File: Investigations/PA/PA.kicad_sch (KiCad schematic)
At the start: 6 parts, among them Q1 BS170

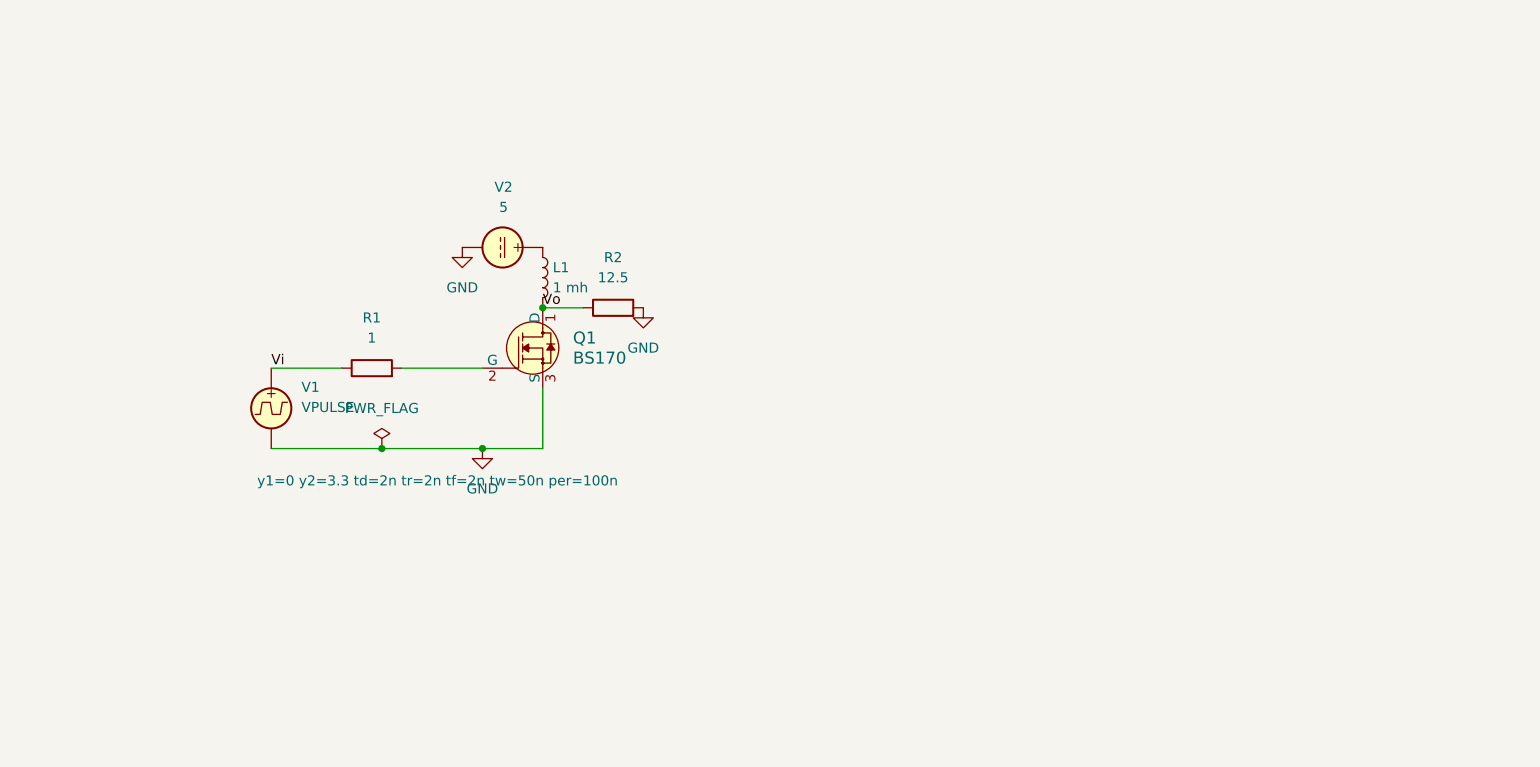
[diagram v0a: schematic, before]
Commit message: Created Pocket FT8 Proto PA
Prototype of a ~1W PA using BS170s with Vcc=5V for a future version of the transceiver.  The low-pass filter can be implemented as a Butterworth with a harmonic trap, or as a Chebyshev without a trap.  Investigations folder has simulations of assorted filter designs/frequencies.
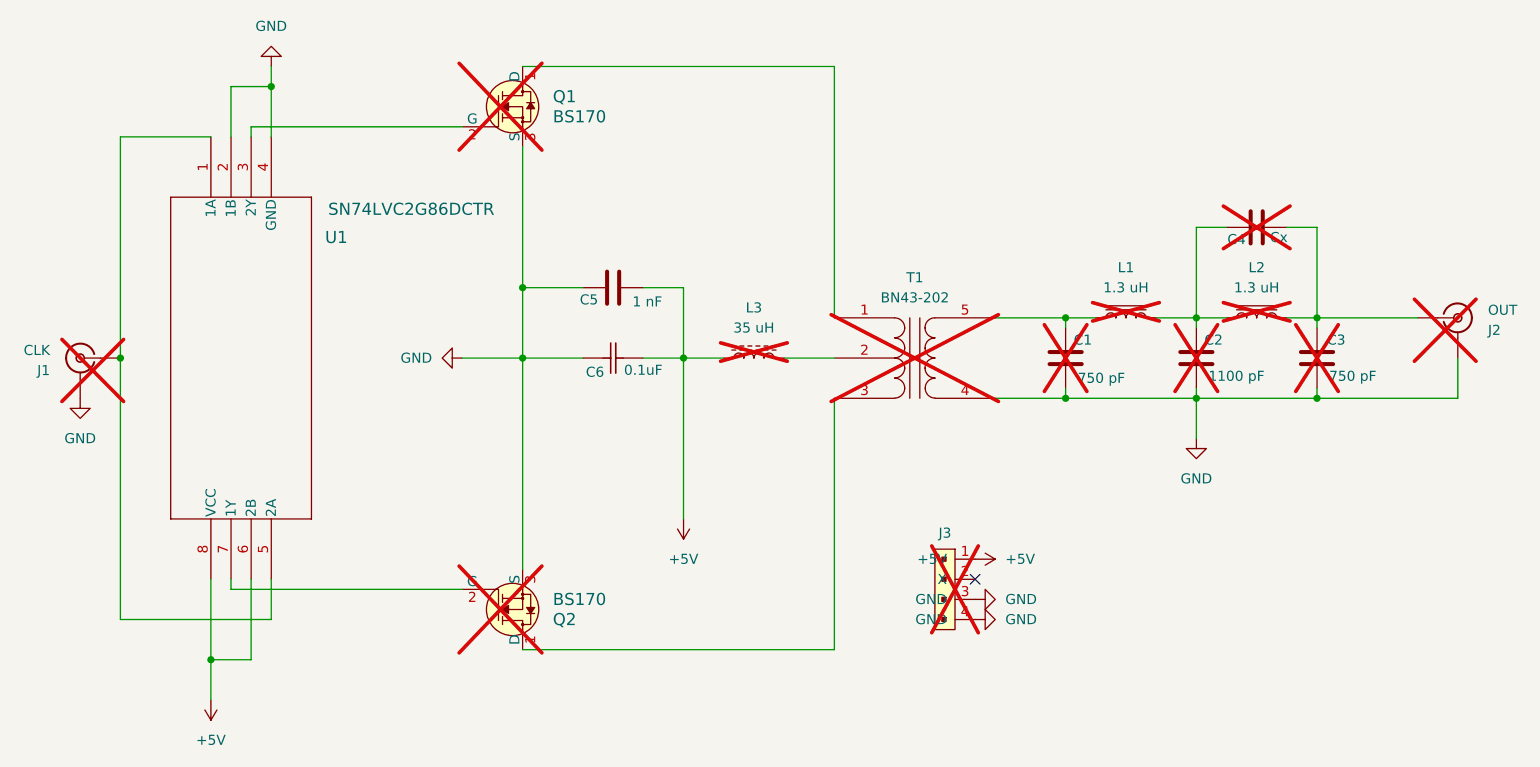
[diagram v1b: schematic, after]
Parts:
- removed L1: 1 mh, symbol Device:L
- removed R1: 1, symbol Device:R
- removed R2: 12.5, symbol Device:R
- removed V1: VPULSE, symbol Simulation_SPICE:VPULSE
- removed V2: 5, symbol Simulation_SPICE:VDC
- added C1, C3: 750 pF, 1210, symbol SparkFun-Capacitor:C
- added C2: 1100 pF, 1210, symbol SparkFun-Capacitor:C
- added C4: Cx, 1210, symbol SparkFun-Capacitor:C
- added C5: 1 nF, 1210, symbol SparkFun-Capacitor:C
- added C6: 0.1uF, 1210, symbol Kemet2024-08-02_22-05-35:C0603C104K4RACTU
- added J1: CLK, SparkFun-Connector:SMA_Edge, symbol SparkFun-RF:SMA_EdgeMount
- added J2: OUT, SparkFun-Connector:SMA_Edge, symbol SparkFun-RF:SMA_EdgeMount
- added J3: 0022232041, digikey-footprints:PinHeader_1x4_P2.54mm_Drill1.02mm, symbol dk_Rectangular-Connectors-Headers-Male-Pins:0022232041
- added L1, L2: 1.3 uH, Inductor_THT:L_Toroid_Vertical_L13.0mm_W6.5mm_P5.60mm, symbol Device:L_Iron
- added L3: 35 uH, Inductor_THT:L_Toroid_Vertical_L14.0mm_W5.6mm_P5.30mm_Bourns_5700, symbol Device:L_Ferrite
- added Q2: BS170, digikey-footprints:TO-92-3, symbol dk_Transistors-FETs-MOSFETs-Single:BS170
- added T1: BN43-202, KiCAD:BN43-202, symbol Device:BN43-202
- added U1: SN74LVC2G86DCTR, DCT8_TEX, symbol 2024-08-19_17-27-05:SN74LVC2G86DCTR
- Q1: Type (none) -> PTH; now not fitted; now left out of the parts list
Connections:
- net GND: now also C1.2, C2.2, C3.2, C5.1, C6.2, J1.2 (Ext), J2.2 (Ext), J3.3 (GND), J3.4 (GND), Q2.3 (S), T1.4 (S1), U1.2 (1B), U1.4 (GND)
- net at Q1.2 (G): now also U1.3 (2Y)
- net Vo: no longer names the net of Q1.1 (D)
- net Vo: now also T1.1 (PR1)
- new net: J1.1 (In), U1.1 (1A), U1.5 (2A)
- new net: Q2.2 (G), U1.7 (1Y)
- new net: Q2.1 (D), T1.3 (PR2)
- new net: C2.1, C4.1, L1.2, L2.1
- new net: C3.1, C4.2, J2.1 (out), L2.2
- new net: C1.1, L1.1, T1.5 (S2)
- new net: L3.2, T1.2 (PM)
- new net +5V: C5.2, C6.1, J3.1 (+5V), L3.1, U1.6 (2B), U1.8 (VCC)
- no-connect marks 0 -> 1

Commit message: PA Proto submitted to PCBWay
First PA Proto uses XOR to generate differentials, (2) BS170 finals, 5Vcc, and Chebyshev LP filter on a 2-Layer Board.
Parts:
- C1, C3: footprint 1210 -> 1206; Tolerance 100% -> 2%; Voltage 1kV -> 100V
- C2: footprint 1210 -> 1206; Tolerance 100% -> 5%; Voltage 1kV -> 50V
- C4: footprint 1210 -> 1206; Notes (none) -> Value to be determined by lab experiment; PROD_ID CAP-00000 -> (none); Tolerance 100% -> (none); Type (none) -> SMD; Voltage 1kV -> (none)
- C5: footprint 1210 -> 0805; Manufacturer (none) -> Kemet; Mfg Kemet -> (none); Mfg Part # (none) -> C0805C102K5RAC7800; Tolerance 5% -> 10%
- C6: footprint 1210 -> 1206; Mfg Part # C1210C104J5GAC7800 -> C1206C104K1RAC7210; Tolerance 5% -> 10%; Voltage 50V -> 100V
- U1: Manufacturer (none) -> Texas Instruments; Mfg Part # (none) -> SN74LVC2G86DCTR
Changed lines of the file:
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@@
 			)
 		)
-		(property "Footprint" "1210"
+		(property "Footprint" "1206"
 			(at 99.06 85.09 0)
 			(effects
@@
 			)
 		)
-		(property "Datasheet" "CAP CER 0.1UF 50V C0G/NP0 1210"
+		(property "Datasheet" "C1206C104K1RAC7210"
 			(at 98.552 82.804 0)
 			(effects
@@
 			)
 		)
-		(property "Description" "CAP CER 0.1UF 50V C0G/NP0 1210"
+		(property "Description" "CAP CER 0.1UF 100V X7R 1206"
 			(at 98.298 87.122 0)
 			(effects
@@
 			)
 		)
-		(property "Voltage" "50V"
+		(property "Voltage" "100V"
 			(at 98.806 78.232 0)
 			(effects
@@
 			)
 		)
-		(property "Tolerance" "5%"
+		(property "Tolerance" "10%"
 			(at 94.234 78.232 0)
 			(effects
@@
 			)
 		)
-		(property "Mfg Part #" "C1210C104J5GAC7800"
+		(property "Mfg Part #" "C1206C104K1RAC7210"
 			(at 97.028 80.772 0)
 			(effects
@@
 			)
 		)
-		(property "Footprint" "1210"
+		(property "Footprint" "0805"
 			(at 107.95 80.3148 0)
 			(effects
@@
 			)
 		)
-		(property "Datasheet" "CAP CER 1000PF 50V C0G/NP0 1210"
+		(property "Datasheet" "CAP CER 1000PF 50V X7R 0805"
 			(at 113.03 80.01 0)
 			(effects
@@
 			)
 		)
-		(property "Description" "CAP CER 1000PF 50V C0G/NP0 1210"
+		(property "Description" "CAP CER 1000PF 50V X7R 0805"
 			(at 115.57 81.28 0)
 			(effects
@@
 			)
 		)
-		(property "Tolerance" "5%"
+		(property "Tolerance" "10%"
 			(at 105.41 81.28 0)
 			(effects
@@
 			)
 		)
-		(property "Mfg" "Kemet"
+		(property "Manufacturer" "Kemet"
+			(at 96.52 81.28 90)
+			(effects
+				(font
+					(size 1.27 1.27)
+				)
+				(hide yes)
+			)
+		)
+		(property "Mfg Part #" "C0805C102K5RAC7800"
 			(at 96.52 81.28 90)
 			(effects
@@
 			)
 		)
+		(property "Manufacturer" "Texas Instruments"
+			(at 45.72 62.23 90)
+			(effects
+				(font
+					(size 1.27 1.27)
+				)
+				(hide yes)
+			)
+		)
+		(property "Mfg Part #" "SN74LVC2G86DCTR"
+			(at 45.72 62.23 90)
+			(effects
+				(font
+					(size 1.27 1.27)
+				)
+				(hide yes)
+			)
+		)
 		(pin "6"
 		)
@@
 			)
 		)
-		(property "Footprint" "1210"
+		(property "Footprint" "1206"
 			(at 186.3852 101.6 0)
 			(effects
@@
 			)
 		)
-		(property "Voltage" "1kV"
+		(property "Voltage" "100V"
 			(at 185.42 96.52 0)
 			(effects
@@
 			)
 		)
-		(property "Tolerance" "100%"
+		(property "Tolerance" "2%"
 			(at 185.42 99.06 0)
 			(effects
@@
 			)
 		)
-		(property "Footprint" "1210"
+		(property "Footprint" "1206"
 			(at 189.23 72.6948 0)
 			(effects
@@
 			)
 		)
-		(property "PROD_ID" "CAP-00000"
-			(at 191.77 73.66 0)
-			(effects
-				(font
-					(size 1.27 1.27)
-				)
-				(hide yes)
-			)
-		)
-		(property "Voltage" "1kV"
+		(property "Voltage" ""
 			(at 184.15 73.66 0)
 			(effects
@@
 			)
 		)
-		(property "Tolerance" "100%"
+		(property "Tolerance" ""
 			(at 186.69 73.66 0)
+			(effects
+				(font
+					(size 1.27 1.27)
+				)
+				(hide yes)
+			)
+		)
+		(property "Type" "SMD"
+			(at 177.8 73.66 90)
+			(effects
+				(font
+					(size 1.27 1.27)
+				)
+				(hide yes)
+			)
+		)
+		(property "Field8" ""
+			(at 177.8 73.66 90)
+			(effects
+				(font
+					(size 1.27 1.27)
+				)
+				(hide yes)
+			)
+		)
+		(property "Notes" "Value to be determined by lab experiment"
+			(at 177.8 73.66 90)
 			(effects
 				(font
@@
 			)
 		)
-		(property "Footprint" "1210"
+		(property "Footprint" "1206"
 			(at 171.1452 101.6 0)
 			(effects
@@
 			)
 		)
-		(property "Voltage" "1kV"
+		(property "Voltage" "50V"
 			(at 170.18 96.52 0)
 			(effects
@@
 			)
 		)
-		(property "Tolerance" "100%"
+		(property "Tolerance" "5%"
 			(at 170.18 99.06 0)
 			(effects
@@
 			)
 		)
-		(property "Footprint" "1210"
+		(property "Footprint" "1206"
 			(at 154.6352 101.6 0)
 			(effects
@@
 			)
 		)
-		(property "Voltage" "1kV"
+		(property "Voltage" "100V"
 			(at 153.67 96.52 0)
 			(effects
@@
 			)
 		)
-		(property "Tolerance" "100%"
+		(property "Tolerance" "2%"
 			(at 153.67 99.06 0)
 			(effects
